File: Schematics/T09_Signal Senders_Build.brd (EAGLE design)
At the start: 88.9 x 66 mm, 41 parts, among them IC1 7805TV, IC2 7805TV, IC3 ATMEGA328, SW1 UNIT_ID, X1 , Y2 16MHz

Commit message: Changed RF_SPI Pinout
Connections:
- net N$34: now also IC3.16; no longer IC3.14
- net N$35: now also IC3.14; no longer IC3.15
- net N$36: now also IC3.15; no longer IC3.16
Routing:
- net N$35: track 45.5 -> 25.4 mm
- net N$34: track 52.5 -> 49.9 mm
- net N$36: track 44.8 -> 42.8 mm

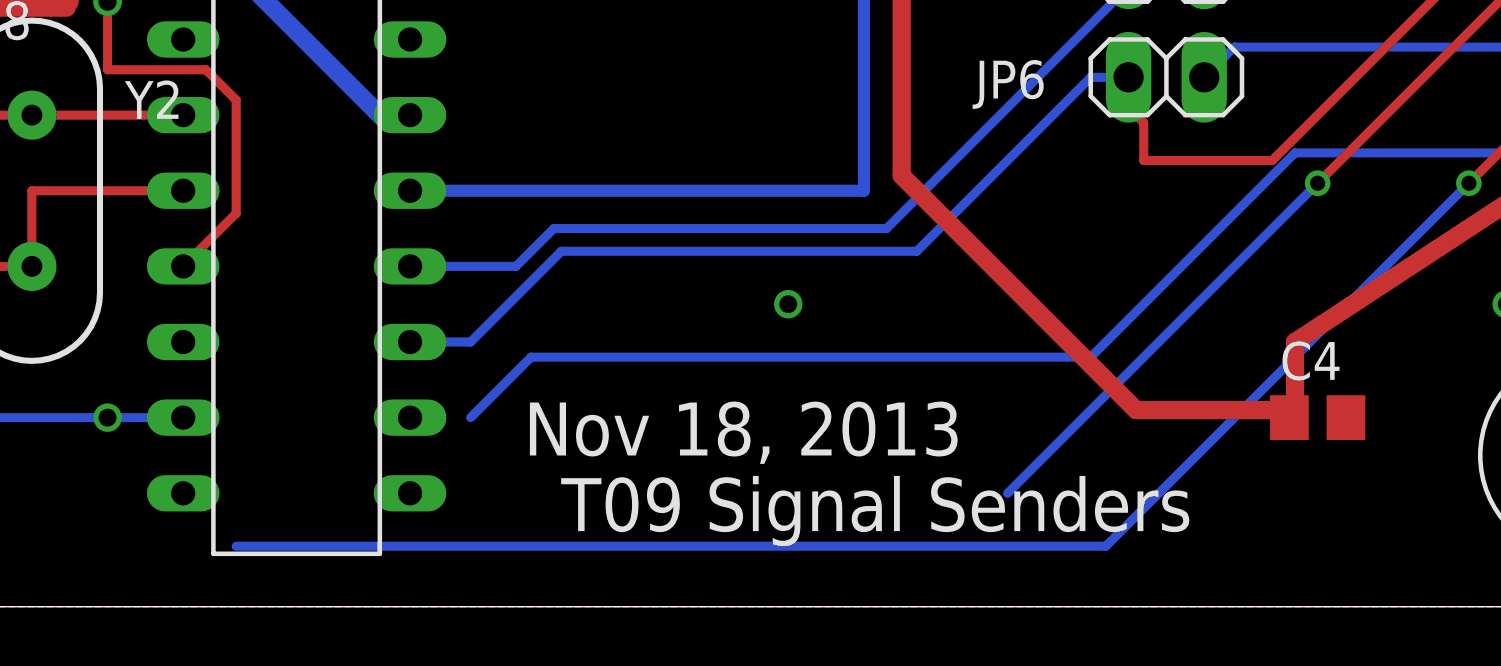
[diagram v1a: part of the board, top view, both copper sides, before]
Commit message: Routed 3 last pins to SPI RF
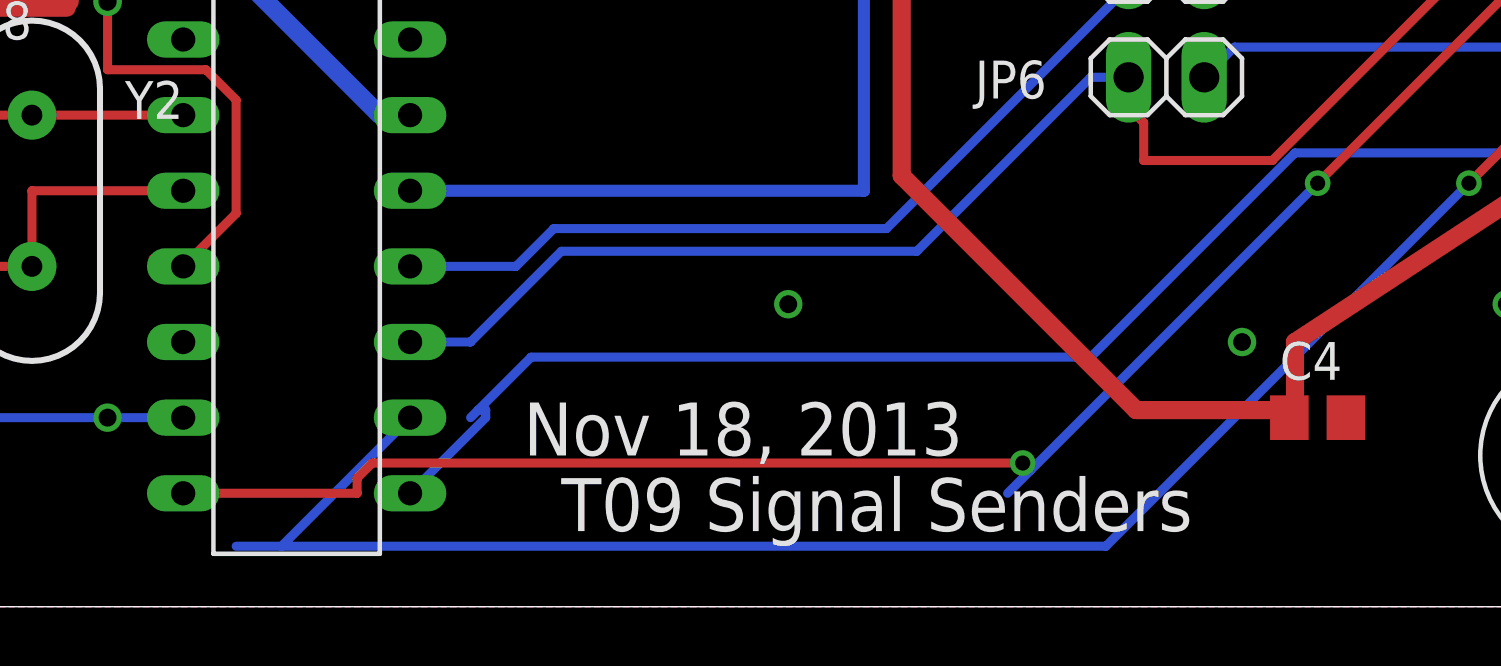
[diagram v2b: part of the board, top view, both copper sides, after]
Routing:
- net N$35: track 25.4 -> 54.7 mm, vias 1 -> 2
- net N$34: track 49.9 -> 56.0 mm
- net N$36: track 42.8 -> 46.9 mm
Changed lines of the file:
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@@
 <?xml version="1.0" encoding="utf-8"?>
 <!DOCTYPE eagle SYSTEM "eagle.dtd">
-<eagle version="6.3">
+<eagle version="6.5.0">
 <drawing>
 <settings>
@@
 <via x="17.78" y="39.37" extent="1-16" drill="0.6"/>
 <via x="58.42" y="48.26" extent="1-16" drill="0.6"/>
+<via x="72.39" y="8.89" extent="1-16" drill="0.6"/>
 </signal>
 <signal name="+5V">
@@
 <signal name="N$34">
 <contactref element="JP1" pad="4"/>
-<wire x1="67.818" y1="2.032" x2="38.608" y2="2.032" width="0.3048" layer="16"/>
+<wire x1="67.818" y1="2.032" x2="40.132" y2="2.032" width="0.3048" layer="16"/>
+<wire x1="40.132" y1="2.032" x2="38.608" y2="2.032" width="0.3048" layer="16"/>
 <wire x1="80.01" y1="14.224" x2="67.818" y2="2.032" width="0.3048" layer="16"/>
 <wire x1="82.296" y1="16.51" x2="80.01" y2="14.224" width="0.3048" layer="1"/>
@@
 <via x="80.01" y="14.224" extent="1-16" drill="0.508"/>
 <contactref element="IC3" pad="16"/>
-<wire x1="38.608" y1="2.032" x2="44.45" y2="6.35" width="0" layer="19" extent="16-16"/>
+<wire x1="40.132" y1="2.032" x2="44.45" y2="6.35" width="0.3048" layer="16"/>
 </signal>
 <signal name="N$35">
 <contactref element="JP1" pad="8"/>
-<wire x1="74.93" y1="14.224" x2="64.516" y2="3.81" width="0.3048" layer="16"/>
+<wire x1="74.93" y1="14.224" x2="65.278" y2="4.572" width="0.3048" layer="16"/>
+<wire x1="65.278" y1="4.572" x2="64.516" y2="3.81" width="0.3048" layer="16"/>
 <wire x1="82.296" y1="21.59" x2="74.93" y2="14.224" width="0.3048" layer="1"/>
 <wire x1="82.55" y1="21.59" x2="82.296" y2="21.59" width="0.3048" layer="1"/>
 <via x="74.93" y="14.224" extent="1-16" drill="0.508"/>
 <contactref element="IC3" pad="14"/>
-<wire x1="36.83" y1="3.81" x2="64.516" y2="3.81" width="0" layer="19" extent="16-16"/>
+<wire x1="42.672" y1="3.81" x2="36.83" y2="3.81" width="0.3048" layer="1"/>
+<wire x1="42.672" y1="4.318" x2="42.672" y2="3.81" width="0.3048" layer="1"/>
+<wire x1="43.18" y1="4.826" x2="42.672" y2="4.318" width="0.3048" layer="1"/>
+<wire x1="65.024" y1="4.826" x2="43.18" y2="4.826" width="0.3048" layer="1"/>
+<wire x1="65.278" y1="4.572" x2="65.024" y2="4.826" width="0.3048" layer="16"/>
+<via x="65.024" y="4.826" extent="1-16" drill="0.508"/>
 </signal>
 <signal name="N$36">
 <contactref element="JP1" pad="3"/>
-<wire x1="48.514" y1="8.382" x2="46.482" y2="6.35" width="0.3048" layer="16"/>
+<wire x1="48.514" y1="8.382" x2="46.736" y2="6.604" width="0.3048" layer="16"/>
+<wire x1="46.736" y1="6.604" x2="46.482" y2="6.35" width="0.3048" layer="16"/>
 <wire x1="67.31" y1="8.382" x2="48.514" y2="8.382" width="0.3048" layer="16"/>
 <wire x1="74.168" y1="15.24" x2="67.31" y2="8.382" width="0.3048" layer="16"/>
@@
 <wire x1="85.09" y1="16.51" x2="84.328" y2="16.51" width="0.3048" layer="16"/>
 <contactref element="IC3" pad="15"/>
-<wire x1="44.45" y1="3.81" x2="46.482" y2="6.35" width="0" layer="19" extent="16-16"/>
+<wire x1="46.99" y1="6.35" x2="44.45" y2="3.81" width="0.3048" layer="16"/>
+<wire x1="46.99" y1="6.604" x2="46.99" y2="6.35" width="0.3048" layer="16"/>
+<wire x1="46.736" y1="6.604" x2="46.99" y2="6.604" width="0.3048" layer="16"/>
 </signal>
 <signal name="N$37">
